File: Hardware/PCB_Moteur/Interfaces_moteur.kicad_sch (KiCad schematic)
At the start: 53 parts, among them J10 Conn_01x02, J11 Conn_01x02, J12 Conn_01x02, J13 Conn_01x02, J14 Conn_01x02, J15 Conn_01x02, J20 BM03B-GHS-TBT, J21 BM03B-GHS-TBT, J22 BM03B-GHS-TBT, J23 BM03B-GHS-TBT, J7 Conn_01x02, J8 Conn_01x02, J9 Conn_01x02, U3 MCP1802T-5002I/OT, U4 LSF0204PWR, U5 ISOW1044

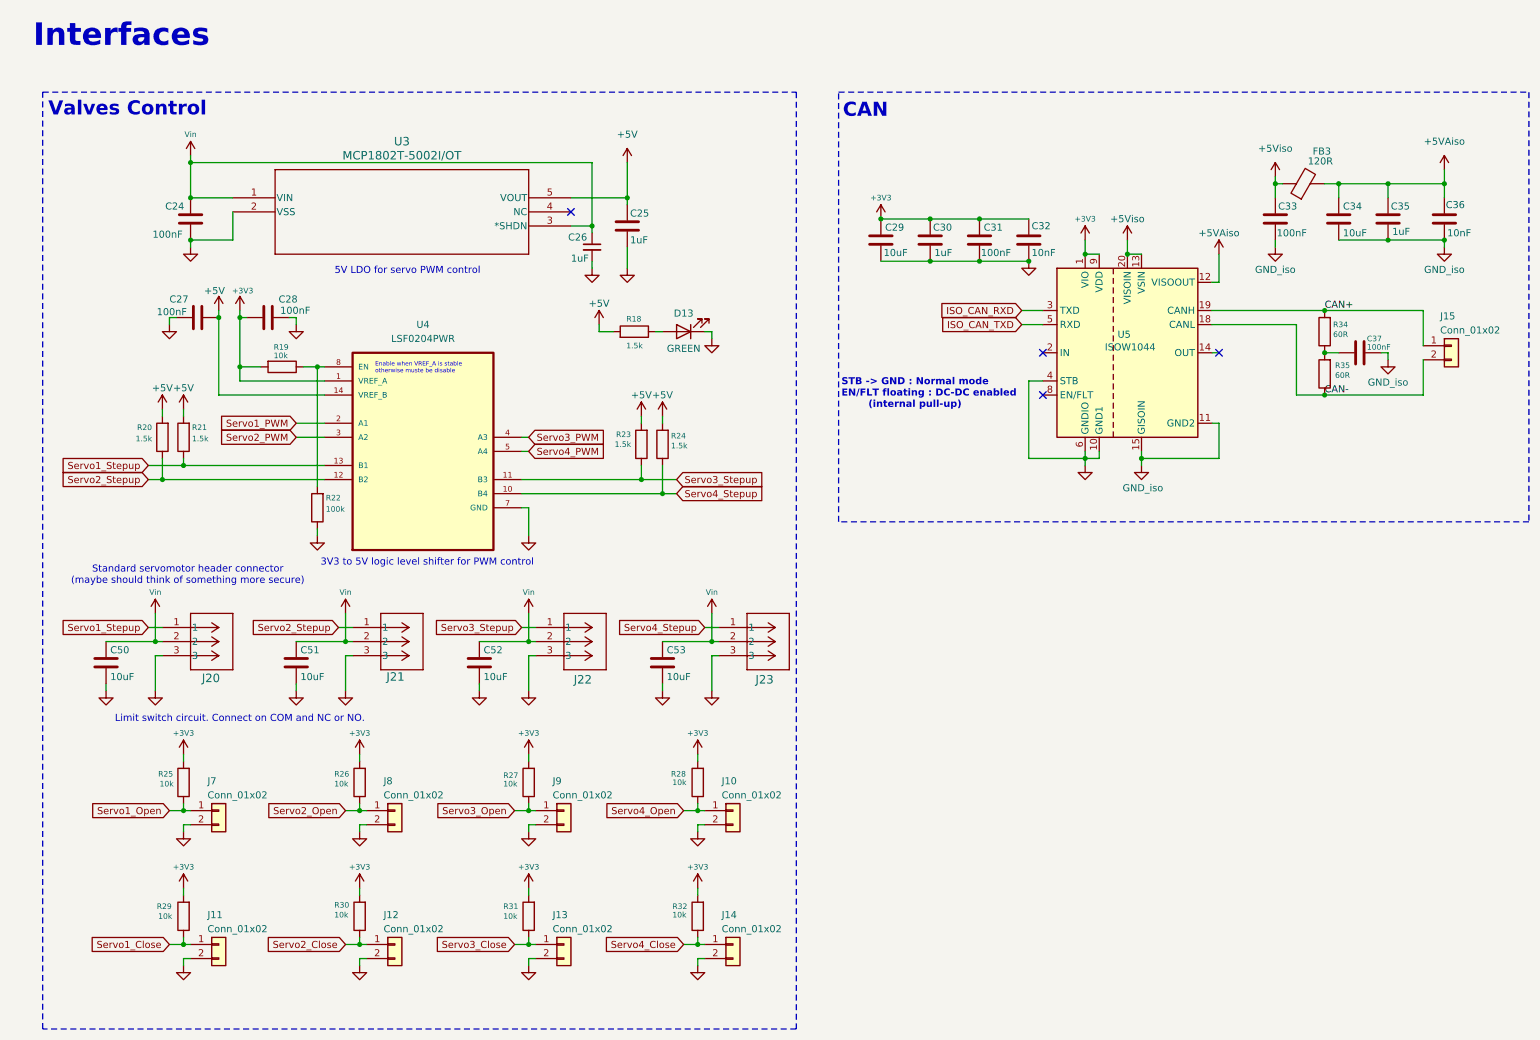
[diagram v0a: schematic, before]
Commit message: wip : work on silkscreen and add all info to BOM
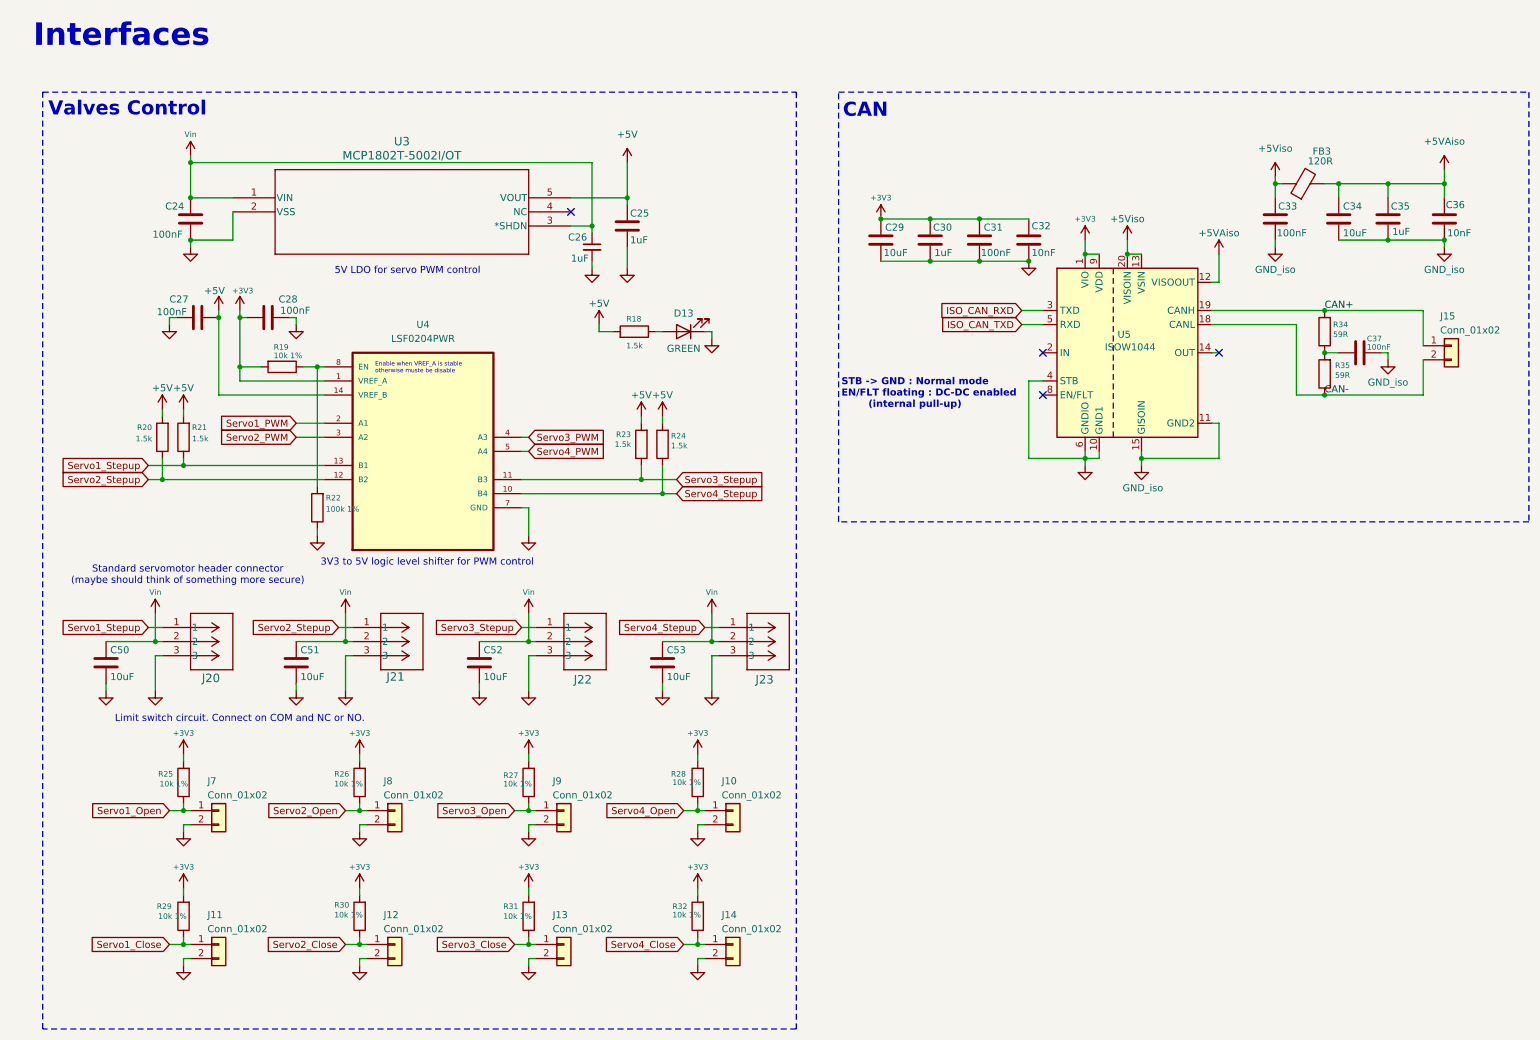
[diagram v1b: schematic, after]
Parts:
- C24, C27, C28, C31, C33, C37: DigiKey_Part_Number (none) -> 399-C0805C104K5RACTUCT-ND; Manufacturer_Part_Number (none) -> C0805C104K5RACTU
- C25, C26, C30, C35: DigiKey_Part_Number (none) -> 399-C0603C105K4RACTUCT-ND; Manufacturer_Part_Number (none) -> C0603C105K4RACTU
- C29, C34, C50, C51, C52, C53: DigiKey_Part_Number (none) -> 1276-2891-1-ND; Manufacturer_Part_Number (none) -> CL21A106KAYNNNE
- C32, C36: DigiKey_Part_Number (none) -> 399-C0603C103K5RACTUCT-ND; Manufacturer_Part_Number (none) -> C0603C103K5RACTU
- FB3: DigiKey_Part_Number (none) -> 1934-1472-1-ND; Manufacturer_Part_Number (none) -> 2508051217Y6
- J10, J11, J12, J13, J14, J7, J8, J9: DigiKey_Part_Number (none) -> A19423-ND; Manufacturer_Part_Number (none) -> 640454-2
- J15: DigiKey_Part_Number (none) -> 900-2189890210CT-ND; Manufacturer_Part_Number (none) -> 2189890210
- J20, J21, J22, J23: DigiKey_Part_Number (none) -> -; Manufacturer_Part_Number (none) -> -
- R18, R20, R21, R23, R24: DigiKey_Part_Number (none) -> P1.5KDBCT-ND; Manufacturer_Part_Number (none) -> ERA-3AEB152V
- R19, R25, R26, R27, R28, R29, R30, R31, R32: value 10k -> 10k 1%; DigiKey_Part_Number (none) -> 541-10.0KCCT-ND; Manufacturer_Part_Number (none) -> CRCW080510K0FKEA
- R22: value 100k -> 100k 1%; DigiKey_Part_Number (none) -> 311-100KCRCT-ND; Manufacturer_Part_Number (none) -> RC0805FR-07100KL
- R34, R35: value 60R -> 59R; DigiKey_Part_Number (none) -> 311-59.0CRCT-ND; Manufacturer_Part_Number (none) -> RC0805FR-0759RL
- U3: DigiKey_Part_Number (none) -> MCP1802T-5002I/OTCT-ND; Manufacturer_Part_Number (none) -> MCP1802T-5002I/OT
- U5: DigiKey_Part_Number (none) -> 296-ISOW1044BDFMRCT-ND; Manufacturer_Part_Number (none) -> ISOW1044BDFMR

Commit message: wip : reorder refdes and fix footprints
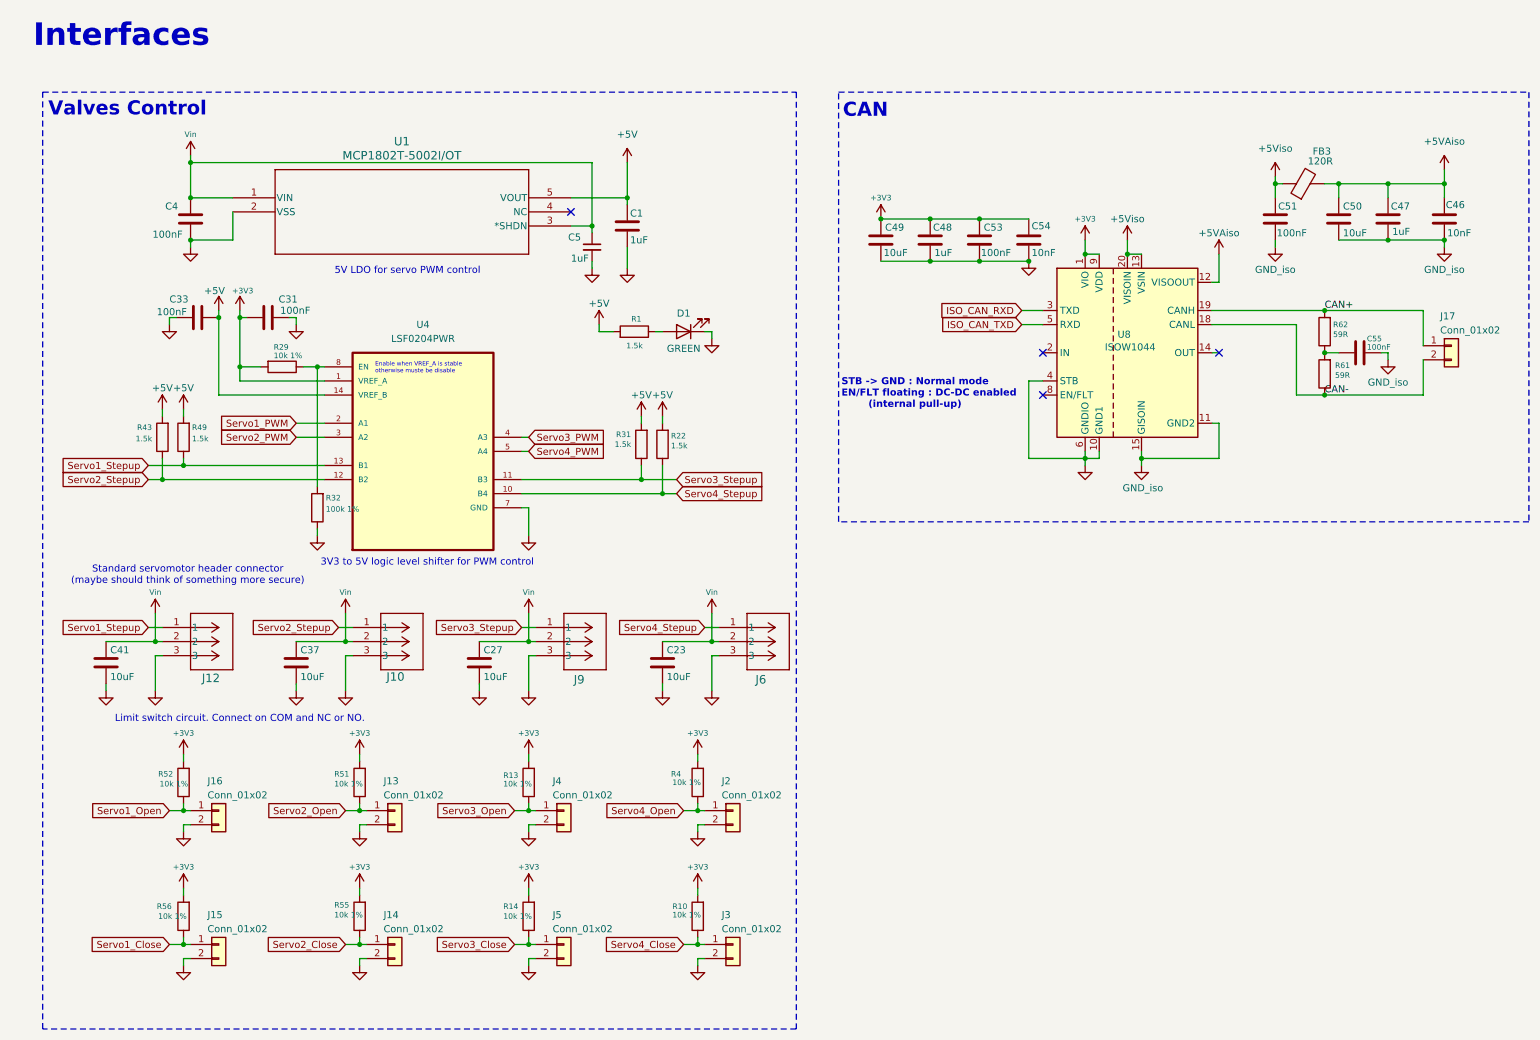
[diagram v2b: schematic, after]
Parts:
- renumbered C25 to C1, C53 to C23, C52 to C27, C28 to C31, C27 to C33, C51 to C37, C24 to C4, C50 to C41, C36 to C46, C35 to C47, C30 to C48, C29 to C49, C26 to C5, C34 to C50, C33 to C51, C31 to C53, C32 to C54, C37 to C55, D13 to D1, J21 to J10, J20 to J12, J8 to J13, J12 to J14, J11 to J15, J7 to J16, J15 to J17, J10 to J2, J14 to J3, J9 to J4, J13 to J5, J23 to J6, J22 to J9, R18 to R1, R32 to R10, R27 to R13, R31 to R14, R24 to R22, R19 to R29, R23 to R31, R22 to R32, R28 to R4, R20 to R43, R21 to R49, R26 to R51, R25 to R52, R30 to R55, R29 to R56, R35 to R61, R34 to R62, U3 to U1, U5 to U8

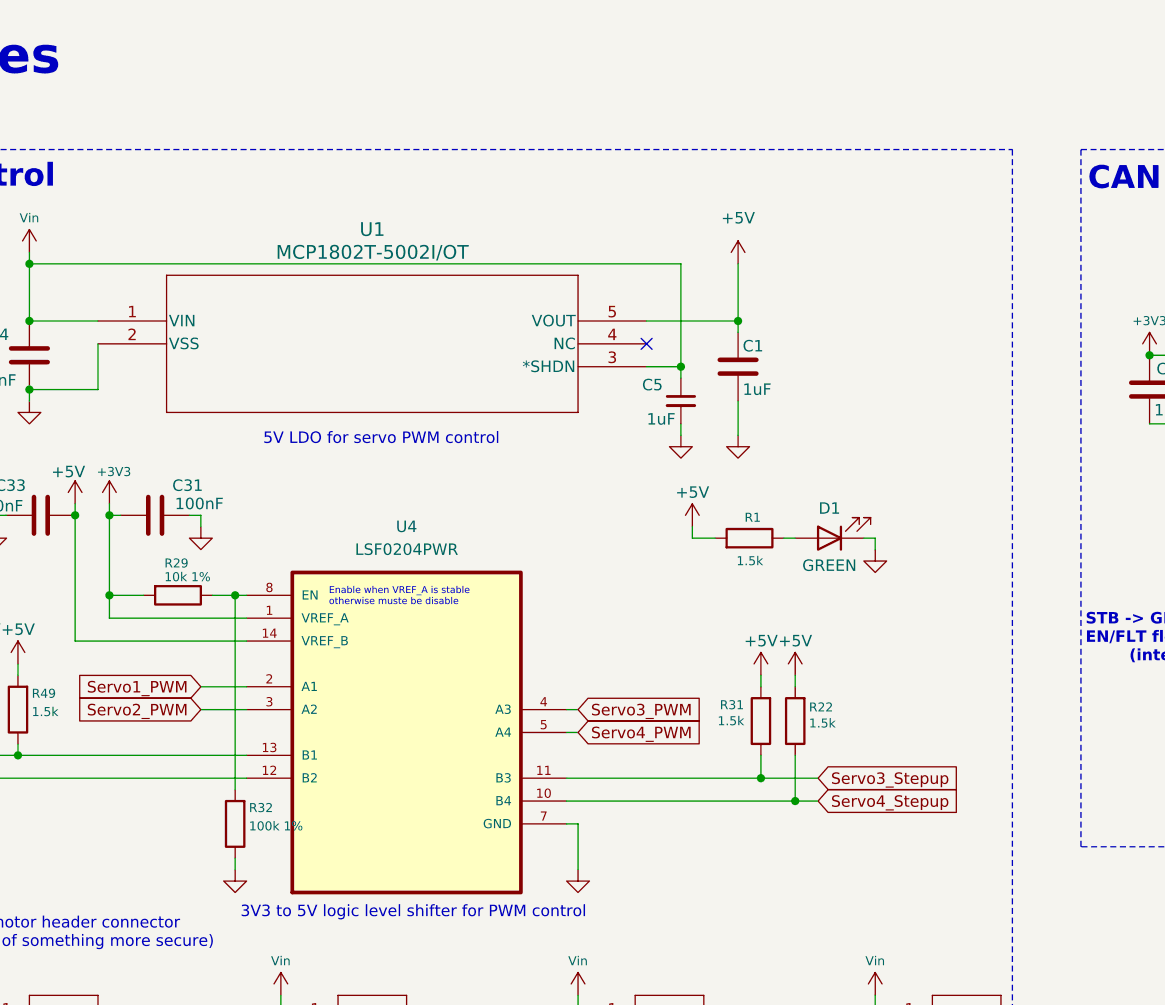
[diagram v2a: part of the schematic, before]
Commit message: fix(moteur + gse): move xt30 to border + fix silkscreen + connect shield to gnd  in pressure sensor + remake rounded corners + fix/add doc
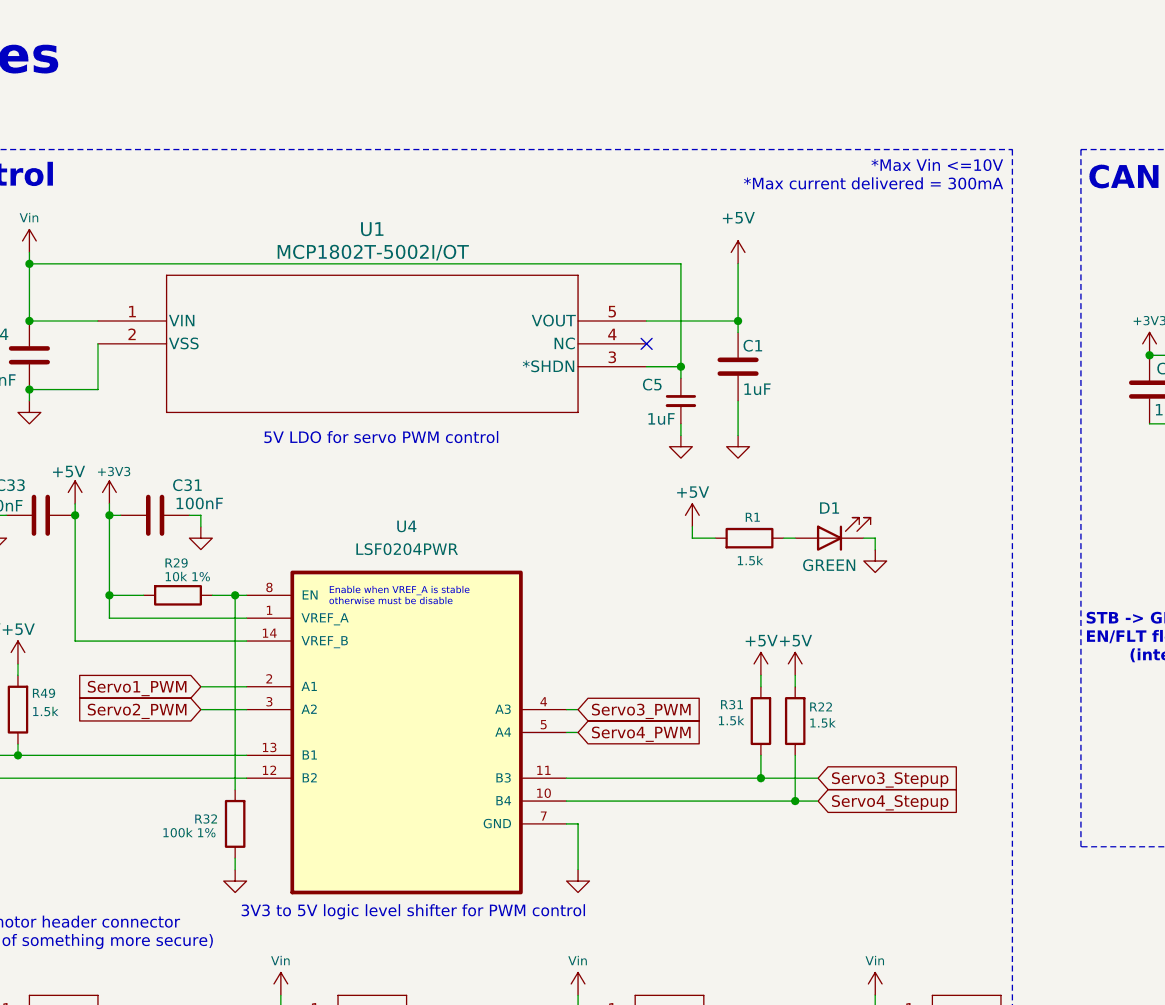
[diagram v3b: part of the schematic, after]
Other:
- note added: "*Max Vin <=10V *Max current delivered = 300mA"
- note added: "Enable when VREF_A is stable otherwise must be disable"
- note removed: "Enable when VREF_A is stable otherwise muste be disable"
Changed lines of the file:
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@@
 		)
 	)
+	(text "*Max Vin <=10V\n*Max current delivered = 300mA"
+		(exclude_from_sim no)
+		(at 150.114 29.718 0)
+		(effects
+			(font
+				(size 1.27 1.27)
+			)
+			(justify right)
+		)
+	)
 	(text "5V LDO for servo PWM control"
 		(exclude_from_sim no)
@@
 		)
 	)
-	(text "Enable when VREF_A is stable\notherwise muste be disable"
+	(text "Enable when VREF_A is stable\notherwise must be disable"
 		(exclude_from_sim no)
 		(at 75.184 76.454 0)
@@
 		(dnp no)
 		(property "Reference" "R32"
-			(at 66.294 99.822 0)
+			(at 60.198 101.092 0)
 			(effects
 				(font
@@
 		)
 		(property "Value" "100k 1%"
-			(at 66.294 101.854 0)
+			(at 56.642 102.616 0)
 			(effects
 				(font
